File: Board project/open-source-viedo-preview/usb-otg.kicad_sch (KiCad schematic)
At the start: 7 parts

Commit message: Imporoved electrical schematic
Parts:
- C2: renamed from C?; footprint (none) -> Capacitor_SMD:C_1812_4532Metric_Pad1.57x3.40mm_HandSolder
- J12: renamed from J?; footprint (none) -> Connector_USB:USB_A_Molex_67643_Horizontal
- R7, R8: renamed from R?; footprint (none) -> Resistor_SMD:R_1206_3216Metric_Pad1.30x1.75mm_HandSolder
- U3, U4: renamed from U?; footprint DBZ3 -> Package_TO_SOT_SMD:SOT-23
- gave numbers to parts that had none: 1
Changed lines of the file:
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@@
 (kicad_sch (version 20201015) (generator eeschema)
+  (page 1 6)
   (paper "A4")
   (junction (at 74.93 95.25) (diameter 1.016) (color 0 0 0 0))
@@
   (symbol (lib_id "power:GND") (at 74.93 97.79 0) (unit 1)
     (in_bom yes) (on_board yes)
-    (property "Reference" "#PWR?" (id 0) (at 74.93 104.14 0)
+    (property "Reference" "#PWR036" (id 0) (at 74.93 104.14 0)
       (effects (font (size 1.27 1.27)) hide)
     )
@@
   (symbol (lib_id "power:GND") (at 148.59 58.42 0) (unit 1)
     (in_bom yes) (on_board yes)
-    (property "Reference" "#PWR?" (id 0) (at 148.59 64.77 0)
+    (property "Reference" "#PWR037" (id 0) (at 148.59 64.77 0)
       (effects (font (size 1.27 1.27)) hide)
     )
@@
   (symbol (lib_id "power:GND") (at 148.59 105.41 0) (unit 1)
     (in_bom yes) (on_board yes)
-    (property "Reference" "#PWR?" (id 0) (at 148.59 111.76 0)
+    (property "Reference" "#PWR038" (id 0) (at 148.59 111.76 0)
       (effects (font (size 1.27 1.27)) hide)
     )
@@
   (symbol (lib_id "power:GND") (at 179.07 105.41 0) (unit 1)
     (in_bom yes) (on_board yes)
-    (property "Reference" "#PWR?" (id 0) (at 179.07 111.76 0)
+    (property "Reference" "#PWR039" (id 0) (at 179.07 111.76 0)
       (effects (font (size 1.27 1.27)) hide)
     )
@@
   (symbol (lib_id "power:GND") (at 205.74 105.41 0) (unit 1)
     (in_bom yes) (on_board yes)
-    (property "Reference" "#PWR?" (id 0) (at 205.74 111.76 0)
+    (property "Reference" "#PWR040" (id 0) (at 205.74 111.76 0)
       (effects (font (size 1.27 1.27)) hide)
     )
@@
   (symbol (lib_id "power:GND") (at 234.95 105.41 0) (unit 1)
     (in_bom yes) (on_board yes)
-    (property "Reference" "#PWR?" (id 0) (at 234.95 111.76 0)
+    (property "Reference" "#PWR041" (id 0) (at 234.95 111.76 0)
       (effects (font (size 1.27 1.27)) hide)
     )
@@
   (symbol (lib_id "Device:R") (at 195.58 77.47 90) (unit 1)
     (in_bom yes) (on_board yes)
-    (property "Reference" "R?" (id 0) (at 195.58 71.12 90))
+    (property "Reference" "R7" (id 0) (at 195.58 71.12 90))
     (property "Value" "10k" (id 1) (at 195.58 73.66 90))
-    (property "Footprint" "" (id 2) (at 195.58 79.248 90)
+    (property "Footprint" "Resistor_SMD:R_1206_3216Metric_Pad1.30x1.75mm_HandSolder" (id 2) (at 195.58 79.248 90)
       (effects (font (size 1.27 1.27)) hide)
     )
@@
   (symbol (lib_id "Device:R") (at 205.74 90.17 0) (unit 1)
     (in_bom yes) (on_board yes)
-    (property "Reference" "R?" (id 0) (at 208.28 88.9 0)
+    (property "Reference" "R8" (id 0) (at 208.28 88.9 0)
       (effects (font (size 1.27 1.27)) (justify left))
     )
@@
       (effects (font (size 1.27 1.27)) (justify left))
     )
-    (property "Footprint" "" (id 2) (at 203.962 90.17 90)
+    (property "Footprint" "Resistor_SMD:R_1206_3216Metric_Pad1.30x1.75mm_HandSolder" (id 2) (at 203.962 90.17 90)
       (effects (font (size 1.27 1.27)) hide)
     )
@@
   (symbol (lib_id "Device:C") (at 179.07 91.44 0) (unit 1)
     (in_bom yes) (on_board yes)
-    (property "Reference" "C?" (id 0) (at 182.88 90.17 0)
+    (property "Reference" "C2" (id 0) (at 182.88 90.17 0)
       (effects (font (size 1.27 1.27)) (justify left))
     )
@@
       (effects (font (size 1.27 1.27)) (justify left))
     )
-    (property "Footprint" "" (id 2) (at 180.0352 95.25 0)
+    (property "Footprint" "Capacitor_SMD:C_1812_4532Metric_Pad1.57x3.40mm_HandSolder" (id 2) (at 180.0352 95.25 0)
       (effects (font (size 1.27 1.27)) hide)
     )
@@
   (symbol (lib_id "Transistor_FET:BSS138PW") (at 232.41 77.47 0) (unit 1)
     (in_bom yes) (on_board yes)
-    (property "Reference" "Q?" (id 0) (at 238.76 76.2 0)
+    (property "Reference" "Q1" (id 0) (at 238.76 76.2 0)
       (effects (font (size 1.27 1.27)) (justify left))
     )
@@
   (symbol (lib_id "Connector:USB_OTG") (at 74.93 82.55 0) (unit 1)
     (in_bom yes) (on_board yes)
-    (property "Reference" "J?" (id 0) (at 77.47 69.85 0))
+    (property "Reference" "J12" (id 0) (at 77.47 69.85 0))
     (property "Value" "USB_OTG" (id 1) (at 77.47 72.39 0))
-    (property "Footprint" "" (id 2) (at 78.74 83.82 0)
+    (property "Footprint" "Connector_USB:USB_A_Molex_67643_Horizontal" (id 2) (at 78.74 83.82 0)
       (effects (font (size 1.27 1.27)) hide)
     )
@@
   (symbol (lib_id "2021-02-13_15-19-31:TPD2E009DBZR") (at 87.63 58.42 0) (unit 1)
     (in_bom yes) (on_board yes)
-    (property "Reference" "U?" (id 0) (at 115.57 48.26 0)
+    (property "Reference" "U3" (id 0) (at 115.57 48.26 0)
       (effects (font (size 1.524 1.524)))
     )
@@
       (effects (font (size 1.524 1.524)))
     )
-    (property "Footprint" "DBZ3" (id 2) (at 115.57 52.324 0)
+    (property "Footprint" "Package_TO_SOT_SMD:SOT-23" (id 2) (at 115.57 52.324 0)
       (effects (font (size 1.524 1.524)) hide)
     )
@@
   (symbol (lib_id "2021-02-13_15-19-31:TPD2E009DBZR") (at 92.71 100.33 0) (mirror x) (unit 1)
     (in_bom yes) (on_board yes)
-    (property "Reference" "U?" (id 0) (at 120.65 110.49 0)
+    (property "Reference" "U4" (id 0) (at 120.65 110.49 0)
       (effects (font (size 1.524 1.524)))
     )
@@
       (effects (font (size 1.524 1.524)))
     )
-    (property "Footprint" "DBZ3" (id 2) (at 120.65 106.426 0)
+    (property "Footprint" "Package_TO_SOT_SMD:SOT-23" (id 2) (at 120.65 106.426 0)
       (effects (font (size 1.524 1.524)) hide)
     )

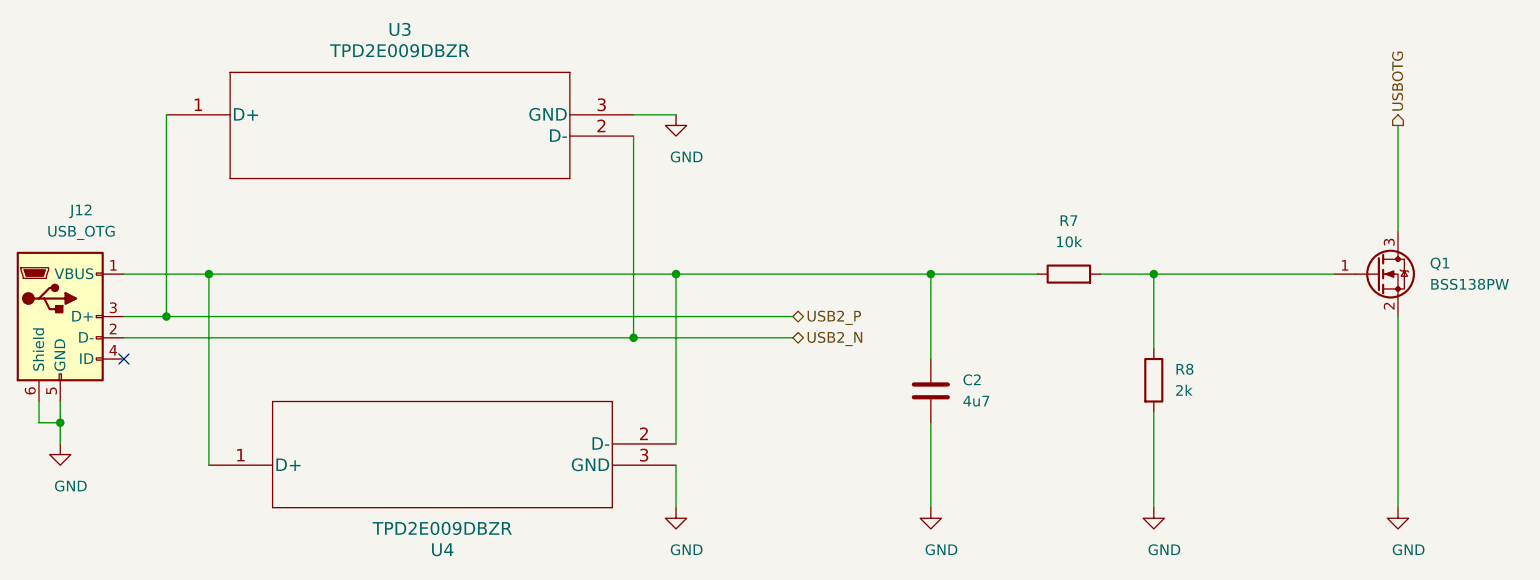
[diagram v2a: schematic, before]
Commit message: ERC error repaired
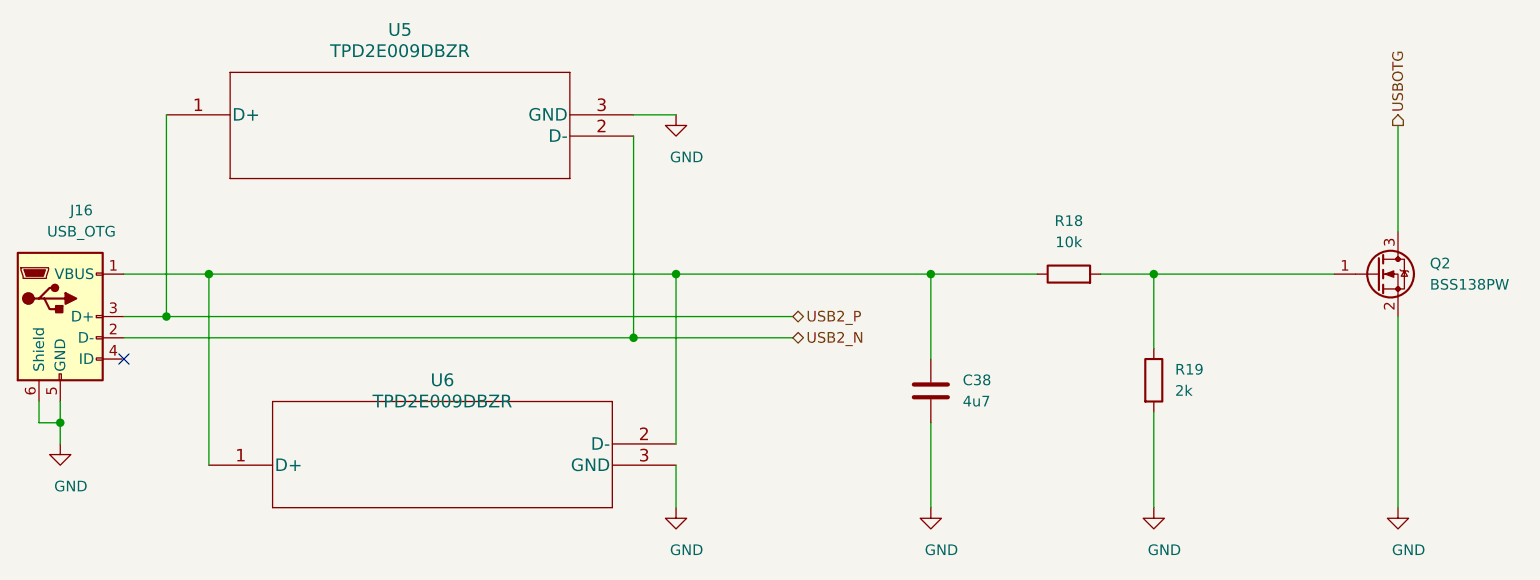
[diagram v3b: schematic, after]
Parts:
- renumbered C2 to C38, J12 to J16, Q1 to Q2, R7 to R18, R8 to R19, U3 to U5, U4 to U6
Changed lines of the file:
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@@
   (symbol (lib_id "power:GND") (at 74.93 97.79 0) (unit 1)
     (in_bom yes) (on_board yes)
-    (property "Reference" "#PWR036" (id 0) (at 74.93 104.14 0)
+    (property "Reference" "#PWR063" (id 0) (at 74.93 104.14 0)
       (effects (font (size 1.27 1.27)) hide)
     )
@@
   (symbol (lib_id "power:GND") (at 148.59 58.42 0) (unit 1)
     (in_bom yes) (on_board yes)
-    (property "Reference" "#PWR037" (id 0) (at 148.59 64.77 0)
+    (property "Reference" "#PWR064" (id 0) (at 148.59 64.77 0)
       (effects (font (size 1.27 1.27)) hide)
     )
@@
   (symbol (lib_id "power:GND") (at 148.59 105.41 0) (unit 1)
     (in_bom yes) (on_board yes)
-    (property "Reference" "#PWR038" (id 0) (at 148.59 111.76 0)
+    (property "Reference" "#PWR065" (id 0) (at 148.59 111.76 0)
       (effects (font (size 1.27 1.27)) hide)
     )
@@
   (symbol (lib_id "power:GND") (at 179.07 105.41 0) (unit 1)
     (in_bom yes) (on_board yes)
-    (property "Reference" "#PWR039" (id 0) (at 179.07 111.76 0)
+    (property "Reference" "#PWR066" (id 0) (at 179.07 111.76 0)
       (effects (font (size 1.27 1.27)) hide)
     )
@@
   (symbol (lib_id "power:GND") (at 205.74 105.41 0) (unit 1)
     (in_bom yes) (on_board yes)
-    (property "Reference" "#PWR040" (id 0) (at 205.74 111.76 0)
+    (property "Reference" "#PWR067" (id 0) (at 205.74 111.76 0)
       (effects (font (size 1.27 1.27)) hide)
     )
@@
   (symbol (lib_id "power:GND") (at 234.95 105.41 0) (unit 1)
     (in_bom yes) (on_board yes)
-    (property "Reference" "#PWR041" (id 0) (at 234.95 111.76 0)
+    (property "Reference" "#PWR068" (id 0) (at 234.95 111.76 0)
       (effects (font (size 1.27 1.27)) hide)
     )
@@
   (symbol (lib_id "Device:R") (at 195.58 77.47 90) (unit 1)
     (in_bom yes) (on_board yes)
-    (property "Reference" "R7" (id 0) (at 195.58 71.12 90))
+    (property "Reference" "R18" (id 0) (at 195.58 71.12 90))
     (property "Value" "10k" (id 1) (at 195.58 73.66 90))
     (property "Footprint" "Resistor_SMD:R_1206_3216Metric_Pad1.30x1.75mm_HandSolder" (id 2) (at 195.58 79.248 90)
@@
   (symbol (lib_id "Device:R") (at 205.74 90.17 0) (unit 1)
     (in_bom yes) (on_board yes)
-    (property "Reference" "R8" (id 0) (at 208.28 88.9 0)
+    (property "Reference" "R19" (id 0) (at 208.28 88.9 0)
       (effects (font (size 1.27 1.27)) (justify left))
     )
@@
   (symbol (lib_id "Device:C") (at 179.07 91.44 0) (unit 1)
     (in_bom yes) (on_board yes)
-    (property "Reference" "C2" (id 0) (at 182.88 90.17 0)
+    (property "Reference" "C38" (id 0) (at 182.88 90.17 0)
       (effects (font (size 1.27 1.27)) (justify left))
     )
@@
   (symbol (lib_id "Transistor_FET:BSS138PW") (at 232.41 77.47 0) (unit 1)
     (in_bom yes) (on_board yes)
-    (property "Reference" "Q1" (id 0) (at 238.76 76.2 0)
+    (property "Reference" "Q2" (id 0) (at 238.76 76.2 0)
       (effects (font (size 1.27 1.27)) (justify left))
     )
@@
   (symbol (lib_id "Connector:USB_OTG") (at 74.93 82.55 0) (unit 1)
     (in_bom yes) (on_board yes)
-    (property "Reference" "J12" (id 0) (at 77.47 69.85 0))
+    (property "Reference" "J16" (id 0) (at 77.47 69.85 0))
     (property "Value" "USB_OTG" (id 1) (at 77.47 72.39 0))
     (property "Footprint" "Connector_USB:USB_A_Molex_67643_Horizontal" (id 2) (at 78.74 83.82 0)
@@
   (symbol (lib_id "2021-02-13_15-19-31:TPD2E009DBZR") (at 87.63 58.42 0) (unit 1)
     (in_bom yes) (on_board yes)
-    (property "Reference" "U3" (id 0) (at 115.57 48.26 0)
+    (property "Reference" "U5" (id 0) (at 115.57 48.26 0)
       (effects (font (size 1.524 1.524)))
     )
@@
     (pin "3")
   )
-  (symbol (lib_id "2021-02-13_15-19-31:TPD2E009DBZR") (at 92.71 100.33 0) (mirror x) (unit 1)
+  (symbol (lib_name "2021-02-13_15-19-31:TPD2E009DBZR_1") (lib_id "2021-02-13_15-19-31:TPD2E009DBZR") (at 92.71 100.33 0) (mirror x) (unit 1)
     (in_bom yes) (on_board yes)
-    (property "Reference" "U4" (id 0) (at 120.65 110.49 0)
+    (property "Reference" "U6" (id 0) (at 120.65 90.17 0)
       (effects (font (size 1.524 1.524)))
     )
-    (property "Value" "TPD2E009DBZR" (id 1) (at 120.65 107.95 0)
+    (property "Value" "TPD2E009DBZR" (id 1) (at 120.65 92.71 0)
       (effects (font (size 1.524 1.524)))
     )
-    (property "Footprint" "Package_TO_SOT_SMD:SOT-23" (id 2) (at 120.65 106.426 0)
+    (property "Footprint" "Package_TO_SOT_SMD:SOT-23" (id 2) (at 120.65 94.234 0)
       (effects (font (size 1.524 1.524)) hide)
     )
